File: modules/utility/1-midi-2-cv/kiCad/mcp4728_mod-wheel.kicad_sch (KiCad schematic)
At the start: 21 parts, among them U5 MCP4728, U6 TL074

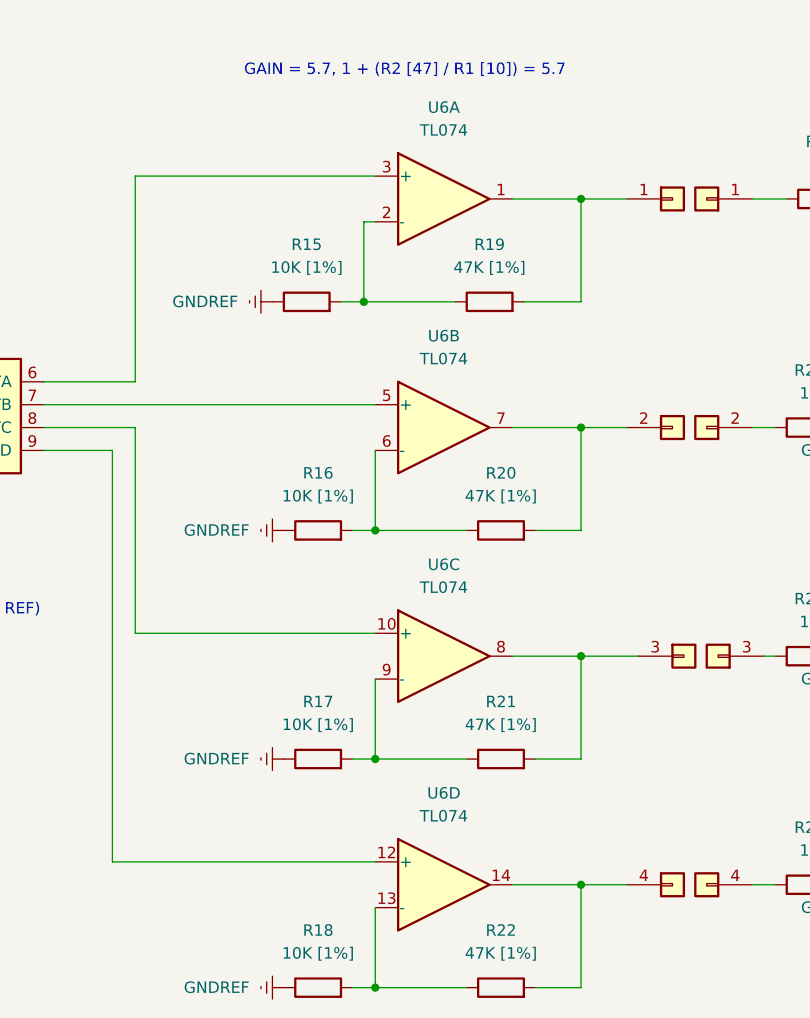
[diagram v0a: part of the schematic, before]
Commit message: Midi 2 CV (Midas) Rework; Delay (Richochet) Rework. Programming, backups for WeAct CV
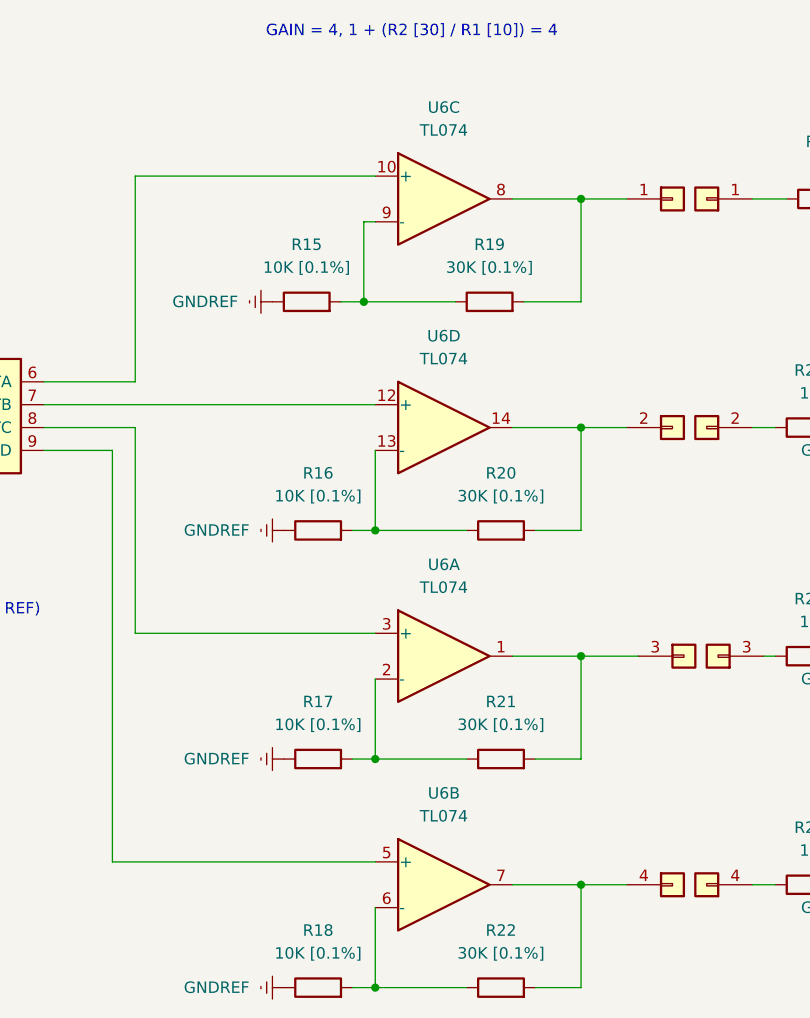
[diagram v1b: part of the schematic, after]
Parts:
- R15, R16, R17, R18: value 10K [1%] -> 10K [0.1%]
- R19, R20, R21, R22: value 47K [1%] -> 30K [0.1%]
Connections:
- net at H5.3 (Pin_3), R21.2: now also U6.1; no longer U6.8
- net at H5.4 (Pin_4), R22.2: now also U6.7; no longer U6.14
- net at R16.2, R20.1: now also U6.13 (-); no longer U6.6 (-)
- net at H5.2 (Pin_2), R20.2: now also U6.14; no longer U6.7
- net at R18.2, R22.1: now also U6.6 (-); no longer U6.13 (-)
- net at R15.2, R19.1: now also U6.9 (-); no longer U6.2 (-)
- net at U5.9 (VOUTD): now also U6.5 (+); no longer U6.12 (+)
- net at H5.1 (Pin_1), R19.2: now also U6.8; no longer U6.1
- net at U5.6 (VOUTA): now also U6.10 (+); no longer U6.3 (+)
- net at U5.7 (VOUTB): now also U6.12 (+); no longer U6.5 (+)
- net at U5.8 (VOUTC): now also U6.3 (+); no longer U6.10 (+)
- net at R17.2, R21.1: now also U6.2 (-); no longer U6.9 (-)
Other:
- note added: "GAIN = 4, 1 + (R2 [30] / R1 [10]) = 4"
- note removed: "GAIN = 5.7, 1 + (R2 [47] / R1 [10]) = 5.7"
- company: (none) -> Lentronics
- title: (none) -> midas_mod-wheel
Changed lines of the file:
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@@
 	(generator "eeschema")
 	(generator_version "8.0")
-	(paper "A4")
+	(paper "A3")
+	(title_block
+		(title "midas_mod-wheel")
+		(date "2024-10-20")
+		(rev "1")
+		(company "Lentronics")
+	)
 	(junction
 		(at 172.72 49.53)
@@
 		)
 	)
-	(text "GAIN = 5.7, 1 + (R2 [47] / R1 [10]) = 5.7"
+	(text "GAIN = 4, 1 + (R2 [30] / R1 [10]) = 4"
 		(exclude_from_sim no)
-		(at 153.162 35.306 0)
+		(at 153.924 30.988 0)
 		(effects
 			(font
@@
 			)
 		)
-		(property "Value" "47K [1%]"
+		(property "Value" "30K [0.1%]"
 			(at 163.83 82.55 90)
 			(effects
@@
 			)
 		)
-		(property "Value" "47K [1%]"
+		(property "Value" "30K [0.1%]"
 			(at 163.83 133.35 90)
 			(effects
@@
 			)
 		)
-		(property "Value" "10K [1%]"
+		(property "Value" "10K [0.1%]"
 			(at 143.51 133.35 90)
 			(effects
@@
 			)
 		)
-		(property "Value" "10K [1%]"
+		(property "Value" "10K [0.1%]"
 			(at 142.24 57.15 90)
 			(effects
@@
 		(lib_id "Amplifier_Operational:TL074")
 		(at 157.48 125.73 0)
-		(unit 4)
+		(unit 2)
 		(exclude_from_sim no)
 		(in_bom yes)
@@
 				(path "/ffcc7acb-943e-4c85-833d-d9691a289ebb/f5a3adbe-4f29-4745-aae4-f507a7b28ec4"
 					(reference "U6")
-					(unit 4)
+					(unit 2)
 				)
 			)
@@
 		(lib_id "Amplifier_Operational:TL074")
 		(at 157.48 74.93 0)
-		(unit 2)
+		(unit 4)
 		(exclude_from_sim no)
 		(in_bom yes)
@@
 				(path "/ffcc7acb-943e-4c85-833d-d9691a289ebb/f5a3adbe-4f29-4745-aae4-f507a7b28ec4"
 					(reference "U6")
-					(unit 2)
+					(unit 4)
 				)
 			)
@@
 		(lib_id "Amplifier_Operational:TL074")
 		(at 157.48 100.33 0)
-		(unit 3)
+		(unit 1)
 		(exclude_from_sim no)
 		(in_bom yes)
@@
 				(path "/ffcc7acb-943e-4c85-833d-d9691a289ebb/f5a3adbe-4f29-4745-aae4-f507a7b28ec4"
 					(reference "U6")
-					(unit 3)
+					(unit 1)
 				)
 			)
@@
 			)
 		)
-		(property "Value" "47K [1%]"
+		(property "Value" "30K [0.1%]"
 			(at 163.83 107.95 90)
 			(effects
@@
 			)
 		)
-		(property "Value" "47K [1%]"
+		(property "Value" "30K [0.1%]"
 			(at 162.56 57.15 90)
 			(effects
@@
 		(lib_id "Amplifier_Operational:TL074")
 		(at 157.48 49.53 0)
-		(unit 1)
+		(unit 3)
 		(exclude_from_sim no)
 		(in_bom yes)
@@
 				(path "/ffcc7acb-943e-4c85-833d-d9691a289ebb/f5a3adbe-4f29-4745-aae4-f507a7b28ec4"
 					(reference "U6")
-					(unit 1)
+					(unit 3)
 				)
 			)
@@
 			)
 		)
-		(property "Value" "10K [1%]"
+		(property "Value" "10K [0.1%]"
 			(at 143.51 107.95 90)
 			(effects
@@
 			)
 		)
-		(property "Value" "10K [1%]"
+		(property "Value" "10K [0.1%]"
 			(at 143.51 82.55 90)
 			(effects

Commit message: finish up PCB finals for run-2, continue on C code for midas/sequencer
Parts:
- U6: footprint Package_SO:SOIC-14_3.9x8.7mm_P1.27mm -> Synth:SOIC-14
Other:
- moved on the sheet: C2, MOD_1, MOD_2, MOD_3, MOD_4, R15, R16, R17, R18, R19, R20, R21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

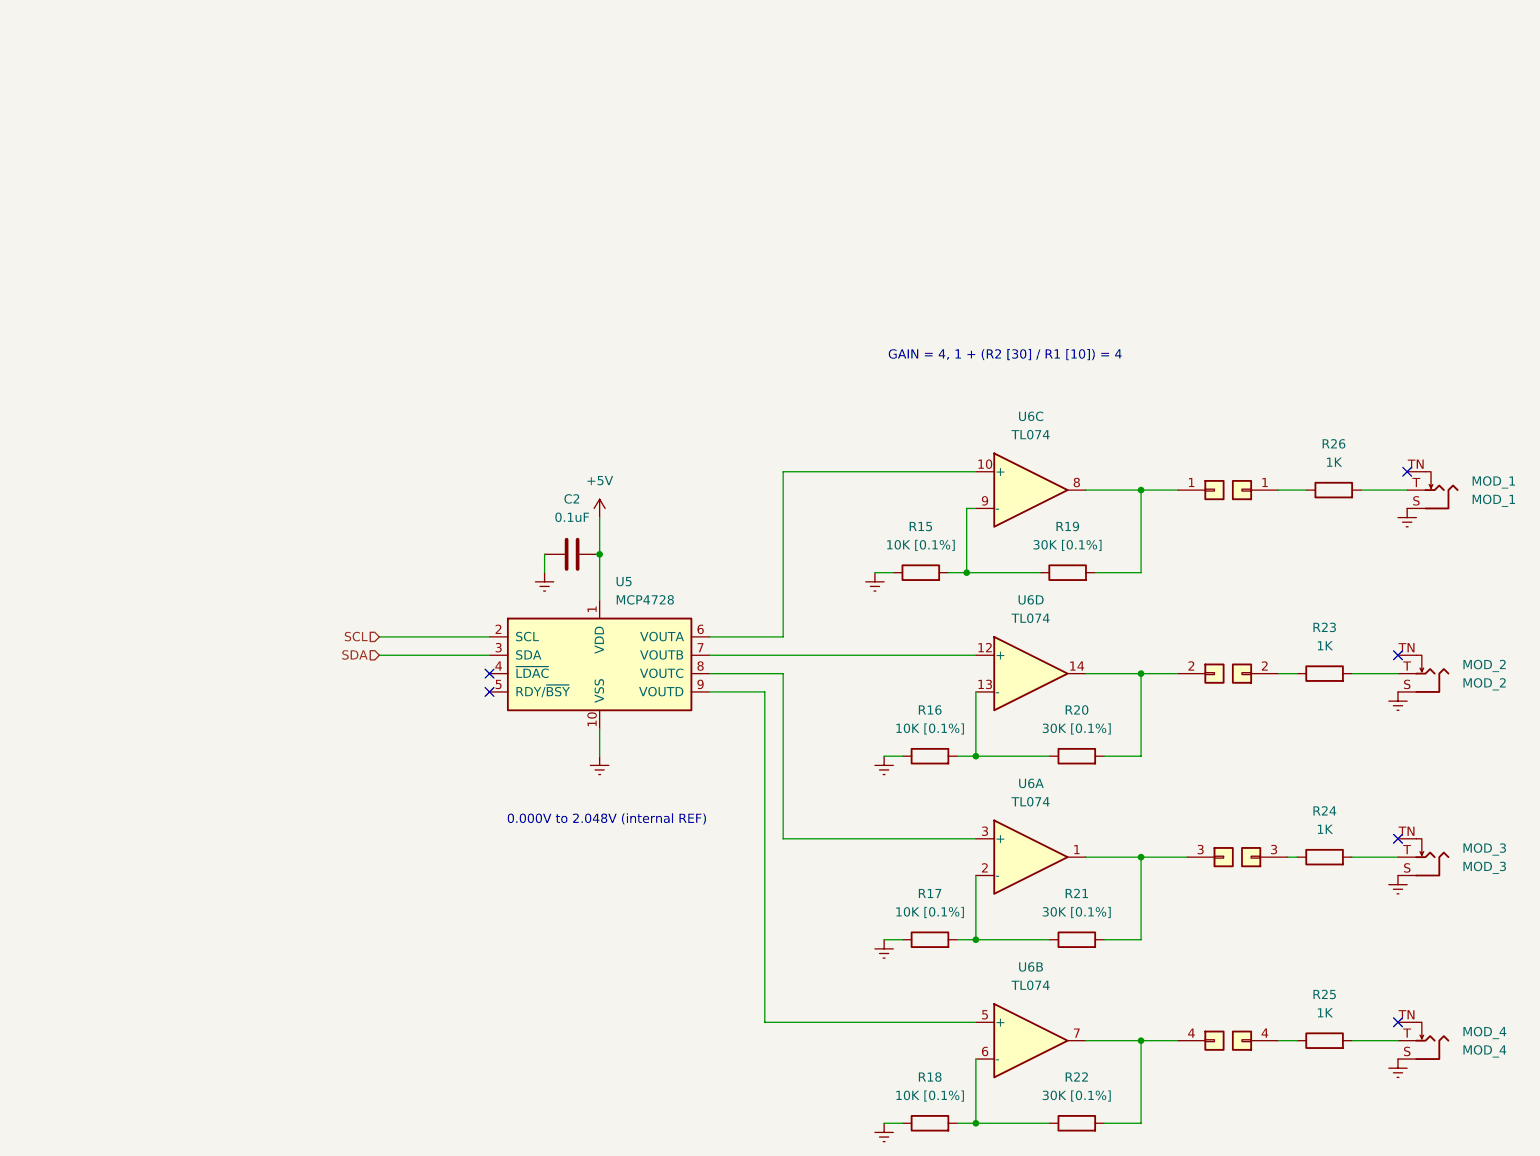
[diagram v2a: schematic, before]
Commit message: debugging and rework for ricochet, midas, wolkje. Added IBOM for drums and other modules.
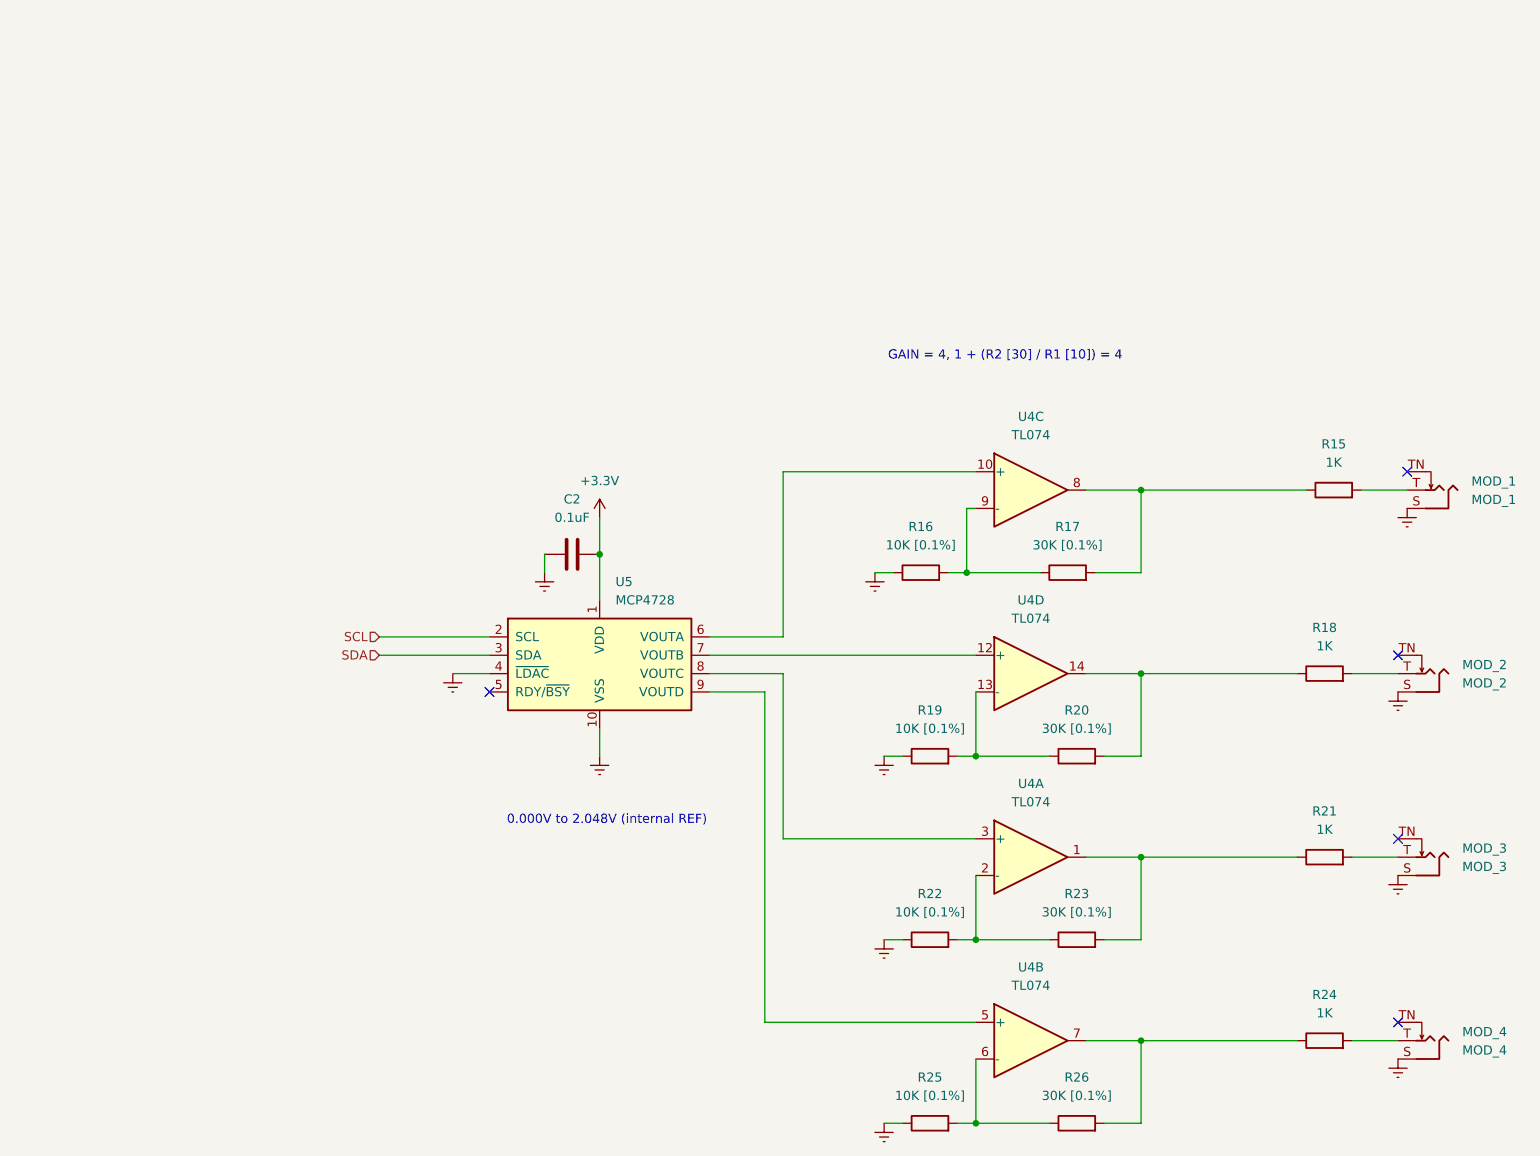
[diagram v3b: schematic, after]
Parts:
- removed H5: PinSocket_01x04, Synth:PinSocket_1x04_P2.54mm_Vertical, symbol synth:PinSocket_01x04
- removed H6: PinHeader_01x04, Synth:PinHeader_1x04_P2.54mm_Vertical, symbol synth:PinHeader_01x04
- renumbered R26 to R15, R15 to R16, R19 to R17, R23 to R18, R16 to R19, R24 to R21, R17 to R22, R21 to R23, R25 to R24, R18 to R25, R22 to R26, U6 to U4
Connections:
- net GNDREF: now also U5.4 (~{LDAC})
- net at R23.2, U4.1: now also R21.1
- net at R15.1: now also R17.2, U4.8
- net at R26.2, U4.7: now also R24.1
- net at R20.2, U4.14: now also R18.1
- net +5V renamed +3.3V
- no-connect marks 6 -> 5
